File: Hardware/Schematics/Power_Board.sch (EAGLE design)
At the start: 82 parts, among them J1 1X2-3.5MM, J2 1X2-3.5MM, J3 1X2-3.5MM, J4 1X2-3.5MM, Q5 4.096MHz, Q8 4.096MHz, Q9 4.096MHz

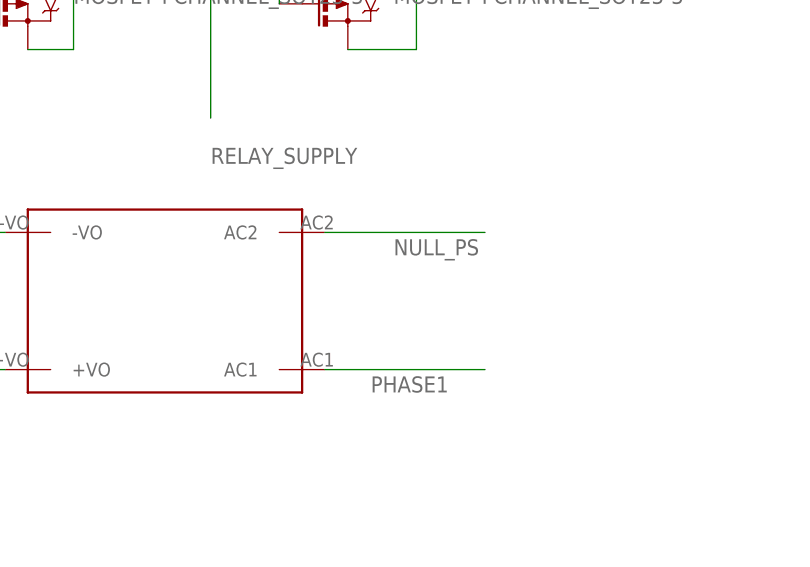
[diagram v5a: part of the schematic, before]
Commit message: Made Logic Board a bit smaller.
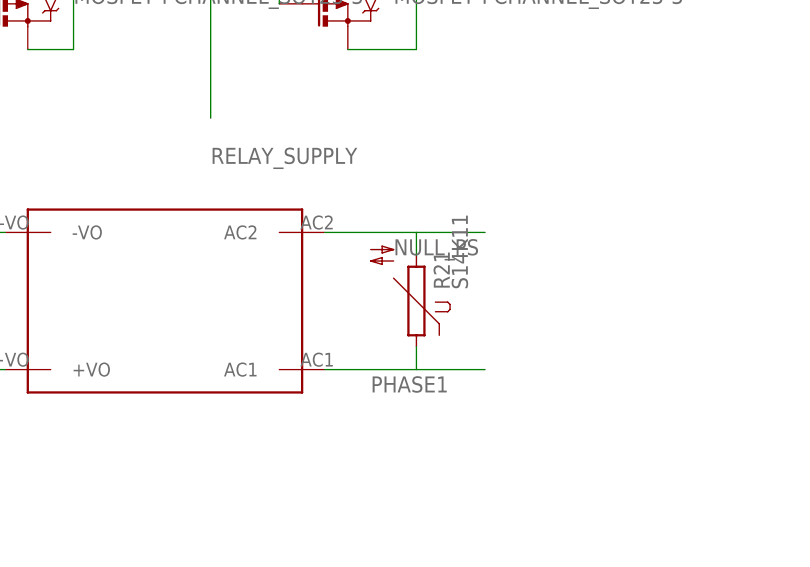
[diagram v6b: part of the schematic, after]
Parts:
- added R21: S14K11, varistor:S14K11
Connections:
- net NULL_PS: now also R21.2
- net PHASE1: now also R21.1
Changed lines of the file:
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@@
 <grid distance="0.1" unitdist="inch" unit="inch" style="lines" multiple="1" display="no" altdistance="0.01" altunitdist="inch" altunit="inch"/>
 <layers>
-<layer number="1" name="Top" color="4" fill="1" visible="no" active="no"/>
-<layer number="2" name="Route2" color="1" fill="3" visible="no" active="no"/>
-<layer number="3" name="Route3" color="4" fill="3" visible="no" active="no"/>
-<layer number="4" name="Route4" color="1" fill="4" visible="no" active="no"/>
-<layer number="5" name="Route5" color="4" fill="4" visible="no" active="no"/>
-<layer number="6" name="Route6" color="1" fill="8" visible="no" active="no"/>
-<layer number="7" name="Route7" color="4" fill="8" visible="no" active="no"/>
-<layer number="8" name="Route8" color="1" fill="2" visible="no" active="no"/>
-<layer number="9" name="Route9" color="4" fill="2" visible="no" active="no"/>
-<layer number="10" name="Route10" color="1" fill="7" visible="no" active="no"/>
-<layer number="11" name="Route11" color="4" fill="7" visible="no" active="no"/>
-<layer number="12" name="Route12" color="1" fill="5" visible="no" active="no"/>
-<layer number="13" name="Route13" color="4" fill="5" visible="no" active="no"/>
-<layer number="14" name="Route14" color="1" fill="6" visible="no" active="no"/>
-<layer number="15" name="Route15" color="4" fill="6" visible="no" active="no"/>
-<layer number="16" name="Bottom" color="1" fill="1" visible="no" active="no"/>
-<layer number="17" name="Pads" color="2" fill="1" visible="no" active="no"/>
-<layer number="18" name="Vias" color="2" fill="1" visible="no" active="no"/>
-<layer number="19" name="Unrouted" color="6" fill="1" visible="no" active="no"/>
-<layer number="20" name="Dimension" color="15" fill="1" visible="no" active="no"/>
-<layer number="21" name="tPlace" color="7" fill="1" visible="no" active="no"/>
-<layer number="22" name="bPlace" color="7" fill="1" visible="no" active="no"/>
-<layer number="23" name="tOrigins" color="15" fill="1" visible="no" active="no"/>
-<layer number="24" name="bOrigins" color="15" fill="1" visible="no" active="no"/>
-<layer number="25" name="tNames" color="7" fill="1" visible="no" active="no"/>
-<layer number="26" name="bNames" color="7" fill="1" visible="no" active="no"/>
-<layer number="27" name="tValues" color="7" fill="1" visible="no" active="no"/>
-<layer number="28" name="bValues" color="7" fill="1" visible="no" active="no"/>
+<layer number="1" name="Top" color="4" fill="1" visible="yes" active="no"/>
+<layer number="2" name="Route2" color="1" fill="3" visible="yes" active="no"/>
+<layer number="3" name="Route3" color="4" fill="3" visible="yes" active="no"/>
+<layer number="4" name="Route4" color="1" fill="4" visible="yes" active="no"/>
+<layer number="5" name="Route5" color="4" fill="4" visible="yes" active="no"/>
+<layer number="6" name="Route6" color="1" fill="8" visible="yes" active="no"/>
+<layer number="7" name="Route7" color="4" fill="8" visible="yes" active="no"/>
+<layer number="8" name="Route8" color="1" fill="2" visible="yes" active="no"/>
+<layer number="9" name="Route9" color="4" fill="2" visible="yes" active="no"/>
+<layer number="10" name="Route10" color="1" fill="7" visible="yes" active="no"/>
+<layer number="11" name="Route11" color="4" fill="7" visible="yes" active="no"/>
+<layer number="12" name="Route12" color="1" fill="5" visible="yes" active="no"/>
+<layer number="13" name="Route13" color="4" fill="5" visible="yes" active="no"/>
+<layer number="14" name="Route14" color="1" fill="6" visible="yes" active="no"/>
+<layer number="15" name="Route15" color="4" fill="6" visible="yes" active="no"/>
+<layer number="16" name="Bottom" color="1" fill="1" visible="yes" active="no"/>
+<layer number="17" name="Pads" color="2" fill="1" visible="yes" active="no"/>
+<layer number="18" name="Vias" color="2" fill="1" visible="yes" active="no"/>
+<layer number="19" name="Unrouted" color="6" fill="1" visible="yes" active="no"/>
+<layer number="20" name="Dimension" color="15" fill="1" visible="yes" active="no"/>
+<layer number="21" name="tPlace" color="7" fill="1" visible="yes" active="no"/>
+<layer number="22" name="bPlace" color="7" fill="1" visible="yes" active="no"/>
+<layer number="23" name="tOrigins" color="15" fill="1" visible="yes" active="no"/>
+<layer number="24" name="bOrigins" color="15" fill="1" visible="yes" active="no"/>
+<layer number="25" name="tNames" color="7" fill="1" visible="yes" active="no"/>
+<layer number="26" name="bNames" color="7" fill="1" visible="yes" active="no"/>
+<layer number="27" name="tValues" color="7" fill="1" visible="yes" active="no"/>
+<layer number="28" name="bValues" color="7" fill="1" visible="yes" active="no"/>
 <layer number="29" name="tStop" color="7" fill="3" visible="no" active="no"/>
 <layer number="30" name="bStop" color="7" fill="6" visible="no" active="no"/>
@@
 <layer number="35" name="tGlue" color="7" fill="4" visible="no" active="no"/>
 <layer number="36" name="bGlue" color="7" fill="5" visible="no" active="no"/>
-<layer number="37" name="tTest" color="7" fill="1" visible="no" active="no"/>
-<layer number="38" name="bTest" color="7" fill="1" visible="no" active="no"/>
+<layer number="37" name="tTest" color="7" fill="1" visible="yes" active="no"/>
+<layer number="38" name="bTest" color="7" fill="1" visible="yes" active="no"/>
 <layer number="39" name="tKeepout" color="4" fill="11" visible="no" active="no"/>
 <layer number="40" name="bKeepout" color="1" fill="11" visible="no" active="no"/>
@@
 <layer number="44" name="Drills" color="7" fill="1" visible="no" active="no"/>
 <layer number="45" name="Holes" color="7" fill="1" visible="no" active="no"/>
-<layer number="46" name="Milling" color="3" fill="1" visible="no" active="no"/>
-<layer number="47" name="Measures" color="7" fill="1" visible="no" active="no"/>
-<layer number="48" name="Document" color="7" fill="1" visible="no" active="no"/>
-<layer number="49" name="Reference" color="7" fill="1" visible="no" active="no"/>
-<layer number="50" name="dxf" color="7" fill="1" visible="no" active="no"/>
-<layer number="51" name="tDocu" color="7" fill="1" visible="no" active="no"/>
-<layer number="52" name="bDocu" color="7" fill="1" visible="no" active="no"/>
-<layer number="53" name="tGND_GNDA" color="7" fill="9" visible="no" active="no"/>
-<layer number="54" name="bGND_GNDA" color="1" fill="9" visible="no" active="no"/>
-<layer number="56" name="wert" color="7" fill="1" visible="no" active="no"/>
-<layer number="57" name="tCAD" color="7" fill="1" visible="no" active="no"/>
-<layer number="59" name="tCarbon" color="7" fill="1" visible="no" active="no"/>
-<layer number="60" name="bCarbon" color="7" fill="1" visible="no" active="no"/>
+<layer number="46" name="Milling" color="3" fill="1" visible="yes" active="no"/>
+<layer number="47" name="Measures" color="7" fill="1" visible="yes" active="no"/>
+<layer number="48" name="Document" color="7" fill="1" visible="yes" active="no"/>
+<layer number="49" name="Reference" color="7" fill="1" visible="yes" active="no"/>
+<layer number="50" name="dxf" color="7" fill="1" visible="yes" active="no"/>
+<layer number="51" name="tDocu" color="7" fill="1" visible="yes" active="no"/>
+<layer number="52" name="bDocu" color="7" fill="1" visible="yes" active="no"/>
+<layer number="53" name="tGND_GNDA" color="7" fill="9" visible="yes" active="no"/>
+<layer number="54" name="bGND_GNDA" color="1" fill="9" visible="yes" active="no"/>
+<layer number="56" name="wert" color="7" fill="1" visible="yes" active="no"/>
+<layer number="57" name="tCAD" color="7" fill="1" visible="yes" active="no"/>
+<layer number="59" name="tCarbon" color="7" fill="1" visible="yes" active="no"/>
+<layer number="60" name="bCarbon" color="7" fill="1" visible="yes" active="no"/>
 <layer number="90" name="Modules" color="5" fill="1" visible="no" active="yes"/>
 <layer number="91" name="Nets" color="2" fill="1" visible="yes" active="yes"/>
@@
 <part name="SUPPLY29" library="supply1" library_urn="urn:adsk.eagle:library:371" deviceset="GND" device=""/>
 <part name="C30" library="rcl" library_urn="urn:adsk.eagle:library:334" deviceset="CPOL-EU" device="E5-6" value="100µF"/>
+<part name="R21" library="varistor" library_urn="urn:adsk.eagle:library:410" deviceset="S14K11" device=""/>
 </parts>
 <sheets>
@@
 <instance part="SUPPLY29" gate="1" x="50.8" y="38.1" rot="R90"/>
 <instance part="C30" gate="G$1" x="48.26" y="129.54" rot="R180"/>
+<instance part="R21" gate="G$1" x="104.14" y="129.54" rot="R90"/>
 </instances>
 <busses>
@@
 <segment>
 <pinref part="U$5" gate="G$1" pin="AC1"/>
-<wire x1="111.76" y1="121.92" x2="93.98" y2="121.92" width="0.1524" layer="91"/>
+<wire x1="111.76" y1="121.92" x2="104.14" y2="121.92" width="0.1524" layer="91"/>
 <label x="99.06" y="119.38" size="1.778" layer="95"/>
+<pinref part="R21" gate="G$1" pin="1"/>
+<wire x1="104.14" y1="121.92" x2="93.98" y2="121.92" width="0.1524" layer="91"/>
+<wire x1="104.14" y1="124.46" x2="104.14" y2="121.92" width="0.1524" layer="91"/>
 </segment>
 </net>
@@
 <segment>
 <pinref part="U$5" gate="G$1" pin="AC2"/>
-<wire x1="93.98" y1="137.16" x2="111.76" y2="137.16" width="0.1524" layer="91"/>
+<wire x1="93.98" y1="137.16" x2="104.14" y2="137.16" width="0.1524" layer="91"/>
 <label x="101.6" y="134.62" size="1.778" layer="95"/>
-</segment>
-</net>
+<pinref part="R21" gate="G$1" pin="2"/>
+<wire x1="104.14" y1="137.16" x2="111.76" y2="137.16" width="0.1524" layer="91"/>
+<wire x1="104.14" y1="134.62" x2="104.14" y2="137.16" width="0.1524" layer="91"/>
+</segment>
+</net>

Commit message: Updated board versions to final (v1) version, and added renders.
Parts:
- JP1: device pinhead:PINHD-2X9/90 -> pinhead:PINHD-2X9
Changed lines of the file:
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@@
 <?xml version="1.0" encoding="utf-8"?>
 <!DOCTYPE eagle SYSTEM "eagle.dtd">
-<eagle version="8.2.1">
+<eagle version="8.2.2">
 <drawing>
 <settings>
@@
 <part name="J2" library="adafruit" deviceset="1X2" device="-3.5MM"/>
 <part name="U$12" library="PowerSocket" deviceset="POWER_SOCKET_EU" device=""/>
-<part name="JP1" library="pinhead" library_urn="urn:adsk.eagle:library:325" deviceset="PINHD-2X9" device="/90"/>
+<part name="JP1" library="pinhead" library_urn="urn:adsk.eagle:library:325" deviceset="PINHD-2X9" device=""/>
 <part name="U$4" library="i2c" deviceset="PCF8574" device="AT"/>
 <part name="SUPPLY8" library="supply1" library_urn="urn:adsk.eagle:library:371" deviceset="GND" device=""/>
